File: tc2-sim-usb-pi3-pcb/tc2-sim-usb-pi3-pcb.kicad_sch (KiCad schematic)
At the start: 5 parts, among them J11 Conn_01x08, J2 Conn_01x03

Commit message: v0.4.0
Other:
- moved on the sheet: J2

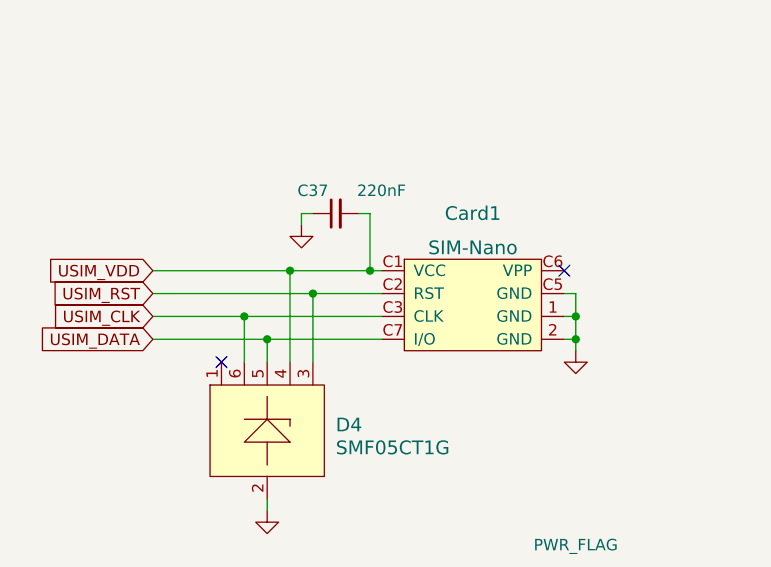
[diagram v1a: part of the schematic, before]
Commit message: Update to use touch sensor
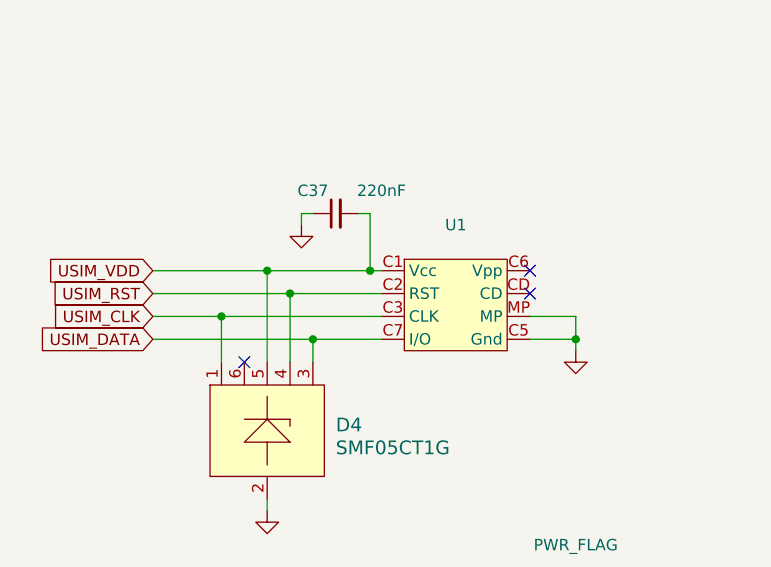
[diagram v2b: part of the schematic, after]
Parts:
- removed Card1: SIM-Nano, cacophony-library:SIM-SMD_SMN-304, symbol cacophony-library:SIM-Nano
- added U1: ~, cacophony-library:K-DYX-010, symbol cacophony-library:K-DYX-010
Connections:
- net GND: now also U1.C5 (Gnd), U1.MP, U1.MP_2 (MP), U1.MP_3 (MP), U1.MP_4 (MP)
- net USIM_CLK: now also D4.1, U1.C3 (CLK); no longer D4.6
- net USIM_DATA: now also D4.3, U1.C7 (I/O); no longer D4.5
- net USIM_RST: now also D4.4, U1.C2 (RST); no longer D4.3
- net USIM_VDD: now also D4.5, U1.C1 (Vcc); no longer D4.4
- no-connect marks 2 -> 3
